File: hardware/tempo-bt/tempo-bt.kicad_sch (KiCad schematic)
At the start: 69 parts, among them J1 JSTPH, J2 USB_C_Receptacle_USB2.0, J3 IO Interfaces, J4 QWIIC_CONNECTORJS-1MM, J5 2x5 PTH ARM CORTEX DEBUG, Q1 DMP3125L-7, SW1 JS102011SAQN, SW2 PTS850, SW3 PTS850, SW4 RESET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

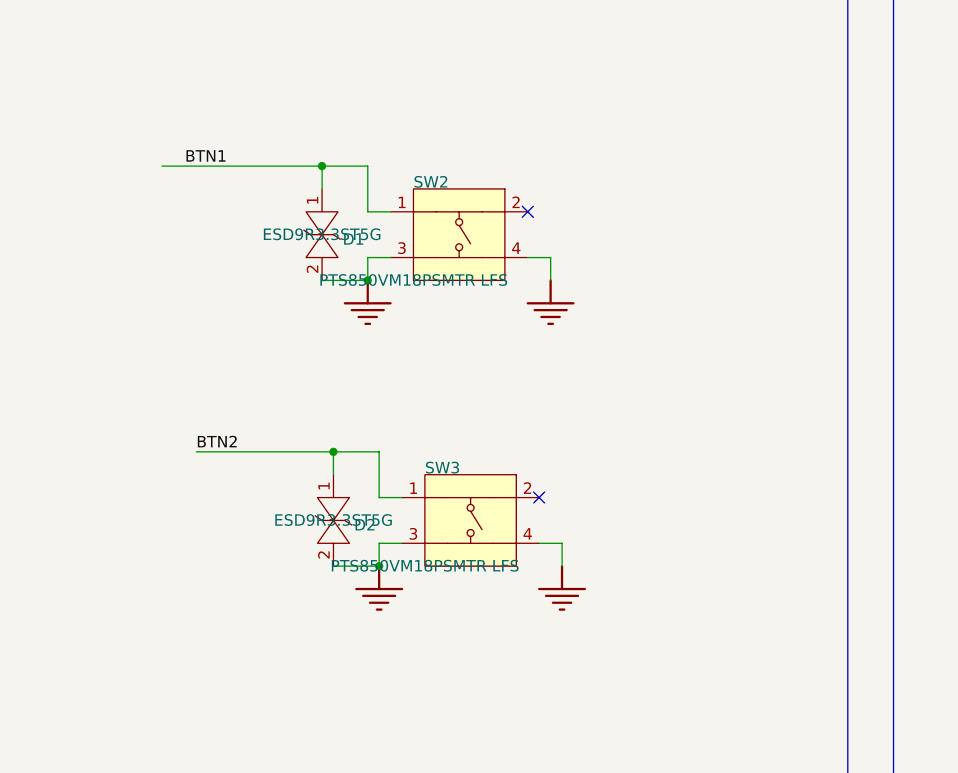
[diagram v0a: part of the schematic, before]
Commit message: Switch orientation incorrect; fixed
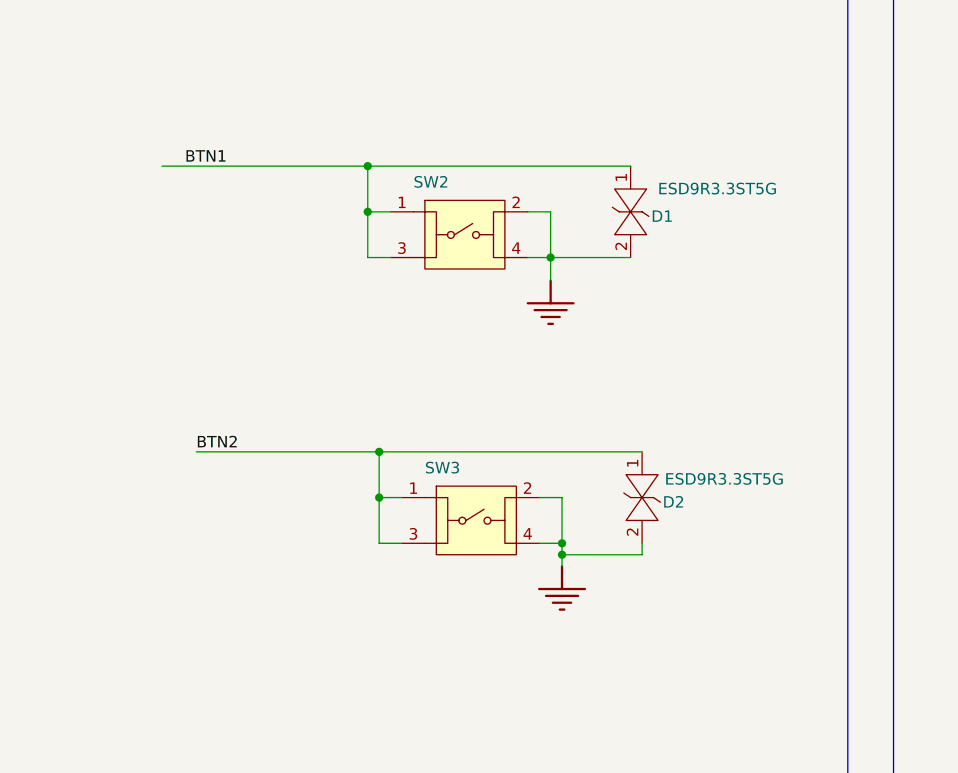
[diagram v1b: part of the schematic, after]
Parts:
- SW2, SW3: symbol nora-altium-import:root_0_SW_TACT_SPST-NO_4Pin -> peakick:PTS850
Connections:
- net BTN1: now also SW2.3
- net BTN2: now also SW3.3
- net GND: now also SW2.2, SW3.2; no longer SW2.3, SW3.3
- no-connect marks 41 -> 39
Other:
- moved on the sheet: D1, D2

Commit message: Through Task 5
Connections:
- net GNSS_TIMEPULSE: now reaches U7.H3 (P0.27/AIN6)
- net GNSS_TIMEPULSE: now also U2.7 (TIMEPULSE)
- net BTN3: no longer names the net of U7.H7 (P0.29)
- no-connect marks 39 -> 37
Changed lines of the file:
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@@
 	)
 	(no_connect
-		(at 389.89 222.25)
-	)
-	(no_connect
 		(at 463.55 171.45)
 	)
@@
 	)
 	(no_connect
-		(at 73.66 41.91)
-	)
-	(no_connect
 		(at 219.71 137.16)
 	)
@@
 	)
 	(no_connect
-		(at 389.89 219.71)
+		(at 389.89 222.25)
 	)
 	(no_connect
@@
 	(wire
 		(pts
-			(xy 389.89 219.71) (xy 407.67 219.71)
-		)
-		(stroke
-			(width 0)
-			(type default)
-		)
-	)
-	(wire
-		(pts
 			(xy 137.16 170.18) (xy 139.7 170.18)
 		)
@@
 	(wire
 		(pts
-			(xy 389.89 222.25) (xy 407.67 222.25)
-		)
-		(stroke
-			(width 0)
-			(type default)
-		)
-	)
-	(wire
-		(pts
 			(xy 408.94 317.5) (xy 424.18 317.5)
 		)
@@
 	(wire
 		(pts
+			(xy 389.89 222.25) (xy 407.67 222.25)
+		)
+		(stroke
+			(width 0)
+			(type default)
+		)
+	)
+	(wire
+		(pts
 			(xy 137.16 251.46) (xy 137.16 255.27)
 		)
@@
 	(wire
 		(pts
+			(xy 389.89 219.71) (xy 407.67 219.71)
+		)
+		(stroke
+			(width 0)
+			(type default)
+		)
+	)
+	(wire
+		(pts
 			(xy 391.16 151.13) (xy 391.16 146.05)
 		)
@@
 		)
 	)
+	(label "GNSS_TIMEPULSE"
+		(at 73.66 41.91 0)
+		(effects
+			(font
+				(size 1.27 1.27)
+			)
+			(justify left bottom)
+		)
+	)
 	(label "D5"
 		(at 199.39 49.53 0)
@@
 		)
 	)
-	(label "BTN3"
-		(at 389.89 224.79 0)
-		(effects
-			(font
-				(size 1.27 1.27)
-			)
-			(justify left bottom)
-		)
-	)
 	(label "SWDCLK"
 		(at 167.64 243.84 0)
@@
 		)
 	)
+	(label "GNSS_TIMEPULSE"
+		(at 389.89 219.71 0)
+		(effects
+			(font
+				(size 1.27 1.27)
+			)
+			(justify left bottom)
+		)
+	)
 	(label "QSPI_CSN"
 		(at 335.28 332.74 0)
@@
 					(size 1.27 1.27)
 				)
+				(hide yes)
 			)
 		)
@@
 					(size 1.27 1.27)
 				)
+				(hide yes)
 			)
 		)
@@
 					(size 1.27 1.27)
 				)
+				(hide yes)
 			)
 		)
@@
 					(size 1.27 1.27)
 				)
+				(hide yes)
 			)
 		)
@@
 					(size 1.27 1.27)
 				)
+				(hide yes)
 			)
 		)
@@
 					(size 1.27 1.27)
 				)
+				(hide yes)
 			)
 		)
@@
 					(size 1.27 1.27)
 				)
+				(hide yes)
 			)
 		)
@@
 					(size 1.27 1.27)
 				)
+				(hide yes)
 			)
 		)
@@
 					(size 1.27 1.27)
 				)
+				(hide yes)
 			)
 		)
@@
 					(size 1.27 1.27)
 				)
+				(hide yes)
 			)
 		)
@@
 					(size 1.27 1.27)
 				)
+				(hide yes)
 			)
 		)
@@
 					(size 1.27 1.27)
 				)
+				(hide yes)
 			)
 		)
@@
 					(size 1.27 1.27)
 				)
+				(hide yes)
 			)
 		)
@@
 					(size 1.27 1.27)
 				)
+				(hide yes)
 			)
 		)
@@
 					(size 1.27 1.27)
 				)
+				(hide yes)
 			)
 		)
@@
 					(size 1.27 1.27)
 				)
+				(hide yes)
 			)
 		)
@@
 					(size 1.27 1.27)
 				)
+				(hide yes)
 			)
 		)
@@
 					(size 1.27 1.27)
 				)
+				(hide yes)
 			)
 		)
@@
 					(size 1.27 1.27)
 				)
+				(hide yes)
 			)
 		)
@@
 					(size 1.27 1.27)
 				)
+				(hide yes)
 			)
 		)
@@
 					(size 1.27 1.27)
 				)
+				(hide yes)
 			)
 		)
@@
 					(size 1.27 1.27)
 				)
+				(hide yes)
 			)
 		)
@@
 					(size 1.27 1.27)
 				)
+				(hide yes)
 			)
 		)
@@
 					(size 1.27 1.27)
 				)
+				(hide yes)
 			)
 		)
@@
 					(size 1.27 1.27)
 				)
+				(hide yes)
 			)
 		)
@@
 					(size 1.27 1.27)
 				)
+				(hide yes)
 			)
 		)
@@
 					(size 1.27 1.27)
 				)
+				(hide yes)
 			)
 		)
@@
 					(size 1.27 1.27)
 				)
+				(hide yes)
 			)
 		)
@@
 					(size 1.27 1.27)
 				)
+				(hide yes)
 			)
 		)
@@
 					(size 1.27 1.27)
 				)
+				(hide yes)
 			)
 		)
@@
 		)
 		(property "MPN" "MX25R6435FZNIL0-TR"
-			(at 370.84 332.74 0)
+			(at 385.572 312.166 0)
 			(effects
 				(font
@@
 					(size 1.27 1.27)
 				)
+				(hide yes)
 			)
 		)
@@
 					(size 1.27 1.27)
 				)
+				(hide yes)
 			)
 		)
@@
 					(size 1.27 1.27)
 				)
+				(hide yes)
 			)
 		)
@@
 					(size 1.27 1.27)
 				)
+				(hide yes)
 			)
 		)
@@
 					(size 1.27 1.27)
 				)
+				(hide yes)
 			)
 		)
@@
 					(size 1.27 1.27)
 				)
+				(hide yes)
 			)
 		)
@@
 					(size 1.27 1.27)
 				)
+				(hide yes)
 			)
 		)
@@
 					(size 1.27 1.27)
 				)
+				(hide yes)
 			)
 		)
@@
 					(size 1.27 1.27)
 				)
+				(hide yes)
 			)
 		)
@@
 					(size 1.27 1.27)
 				)
+				(hide yes)
 			)
 		)
